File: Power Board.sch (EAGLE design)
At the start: 44 parts, among them IC1 SN74LS00N, Q1 IRLB8743PBF, U1 S18V20F12, U2 D24V22F3, U3 D24V22F5

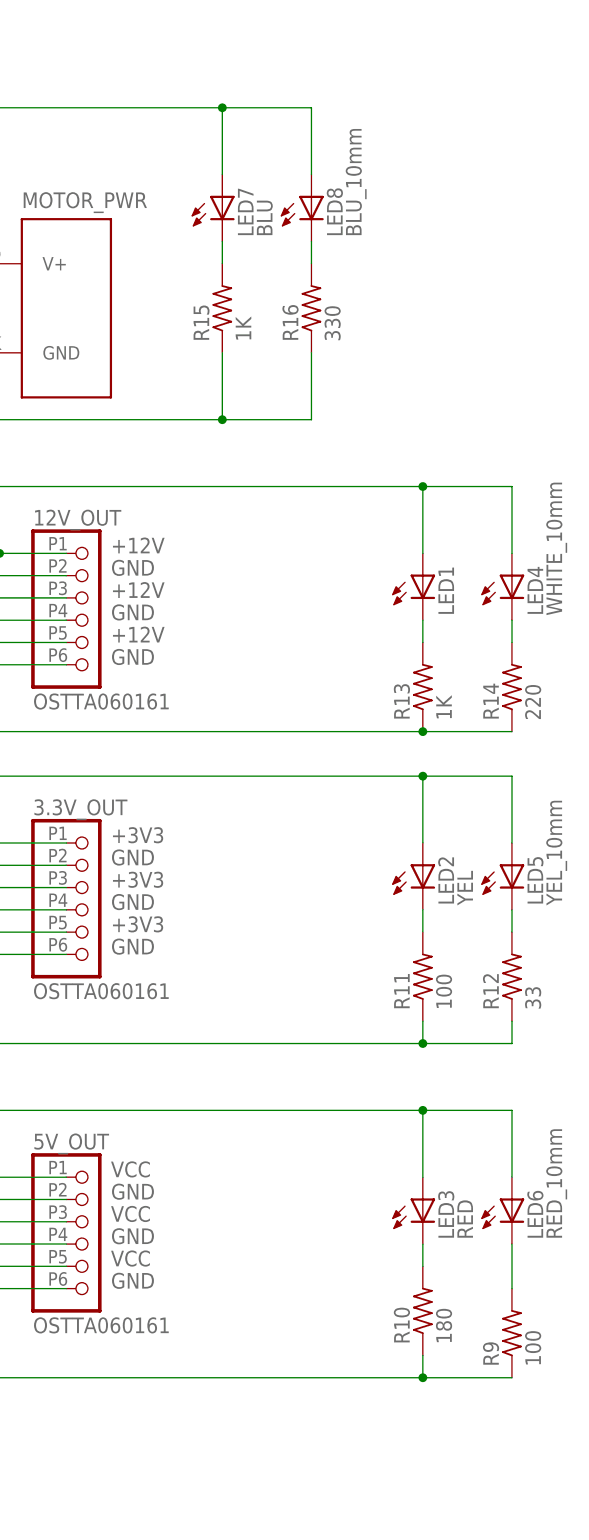
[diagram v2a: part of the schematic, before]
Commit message: Remove large LEDs (they were too hard to find, and produced too much heat)
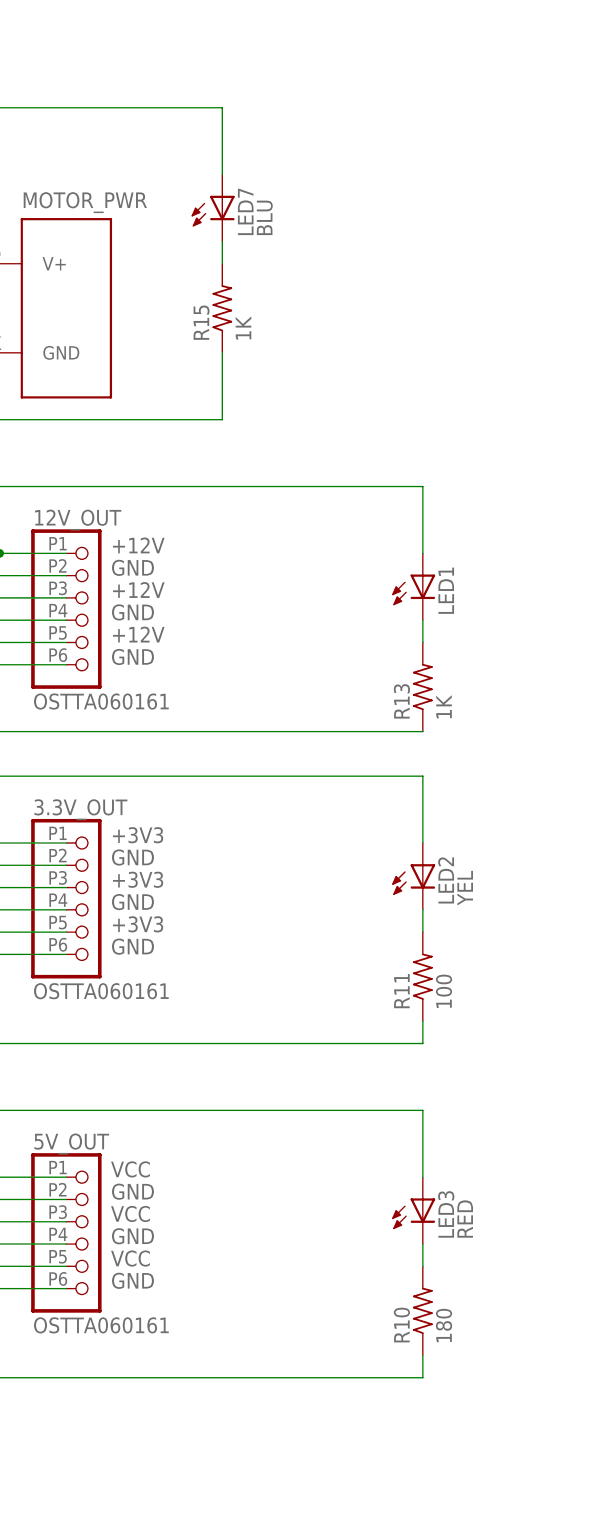
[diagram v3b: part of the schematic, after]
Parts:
- removed LED4: WHITE_10mm, led:LED10MM
- removed LED5: YEL_10mm, Power Board Custom:SPARKFUN_10MMLED
- removed LED6: RED_10mm, Power Board Custom:SPARKFUN_10MMLED
- removed LED8: BLU_10mm, led:LED10MM
- removed R12: 33, resistor:R-US_0207/10
- removed R14: 220, resistor:R-US_0207/10
- removed R16: 330, resistor:R-US_0207/10
- removed R9: 100, resistor:R-US_0207/10
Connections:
- removed net N$11: LED4.C, R14.2
- removed net N$14: LED8.C, R16.2
- removed net N$5: LED6.C, R9.2
- removed net N$9: LED5.C, R12.2
- net +12V: no longer LED4.A
- net +3V3: no longer LED5.A
- net GND: no longer R12.1, R14.1, R9.1
- net MOTOR_0V: no longer R16.1
- net MOTOR_V+: no longer LED8.A
- net VCC: no longer LED6.A
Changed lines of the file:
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@@
 <?xml version="1.0" encoding="utf-8"?>
 <!DOCTYPE eagle SYSTEM "eagle.dtd">
-<eagle version="8.4.0">
+<eagle version="8.6.1">
 <drawing>
 <settings>
-<setting alwaysvectorfont="no"/>
+<setting alwaysvectorfont="yes"/>
 <setting verticaltext="up"/>
 </settings>
@@
 <part name="LED2" library="led" library_urn="urn:adsk.eagle:library:259" deviceset="LED" device="5MM" package3d_urn="urn:adsk.eagle:package:15799/1" value="YEL"/>
 <part name="LED3" library="led" library_urn="urn:adsk.eagle:library:259" deviceset="LED" device="5MM" package3d_urn="urn:adsk.eagle:package:15799/1" value="RED"/>
-<part name="LED5" library="Power Board Custom" deviceset="SPARKFUN_10MMLED" device="" value="YEL_10mm"/>
-<part name="LED6" library="Power Board Custom" deviceset="SPARKFUN_10MMLED" device="" value="RED_10mm"/>
-<part name="R9" library="resistor" library_urn="urn:adsk.eagle:library:348" deviceset="R-US_" device="0207/10" package3d_urn="urn:adsk.eagle:package:25939/1" value="100"/>
 <part name="R10" library="resistor" library_urn="urn:adsk.eagle:library:348" deviceset="R-US_" device="0207/10" package3d_urn="urn:adsk.eagle:package:25939/1" value="180"/>
 <part name="R11" library="resistor" library_urn="urn:adsk.eagle:library:348" deviceset="R-US_" device="0207/10" package3d_urn="urn:adsk.eagle:package:25939/1" value="100"/>
-<part name="R12" library="resistor" library_urn="urn:adsk.eagle:library:348" deviceset="R-US_" device="0207/10" package3d_urn="urn:adsk.eagle:package:25939/1" value="33"/>
 <part name="R13" library="resistor" library_urn="urn:adsk.eagle:library:348" deviceset="R-US_" device="0207/10" package3d_urn="urn:adsk.eagle:package:25939/1" value="1K"/>
-<part name="R14" library="resistor" library_urn="urn:adsk.eagle:library:348" deviceset="R-US_" device="0207/10" package3d_urn="urn:adsk.eagle:package:25939/1" value="220"/>
 <part name="R15" library="resistor" library_urn="urn:adsk.eagle:library:348" deviceset="R-US_" device="0207/10" package3d_urn="urn:adsk.eagle:package:25939/1" value="1K"/>
-<part name="R16" library="resistor" library_urn="urn:adsk.eagle:library:348" deviceset="R-US_" device="0207/10" package3d_urn="urn:adsk.eagle:package:25939/1" value="330"/>
 <part name="LED7" library="led" library_urn="urn:adsk.eagle:library:259" deviceset="LED" device="5MM" package3d_urn="urn:adsk.eagle:package:15799/1" value="BLU"/>
-<part name="LED8" library="led" library_urn="urn:adsk.eagle:library:259" deviceset="LED" device="10MM" package3d_urn="urn:adsk.eagle:package:15828/1" value="BLU_10mm"/>
-<part name="LED4" library="led" library_urn="urn:adsk.eagle:library:259" deviceset="LED" device="10MM" package3d_urn="urn:adsk.eagle:package:15828/1" value="WHITE_10mm"/>
 </parts>
 <sheets>
@@
 <instance part="LED2" gate="G$1" x="236.22" y="132.08"/>
 <instance part="LED3" gate="G$1" x="236.22" y="93.98"/>
-<instance part="LED5" gate="G$1" x="246.38" y="132.08"/>
-<instance part="LED6" gate="G$1" x="246.38" y="93.98"/>
-<instance part="R9" gate="G$1" x="246.38" y="78.74" rot="R90"/>
 <instance part="R10" gate="G$1" x="236.22" y="81.28" rot="R90"/>
 <instance part="R11" gate="G$1" x="236.22" y="119.38" rot="R90"/>
-<instance part="R12" gate="G$1" x="246.38" y="119.38" rot="R90"/>
 <instance part="R13" gate="G$1" x="236.22" y="152.4" rot="R90"/>
-<instance part="R14" gate="G$1" x="246.38" y="152.4" rot="R90"/>
 <instance part="R15" gate="G$1" x="213.36" y="195.58" rot="R90"/>
-<instance part="R16" gate="G$1" x="223.52" y="195.58" rot="R90"/>
 <instance part="LED7" gate="G$1" x="213.36" y="208.28"/>
-<instance part="LED8" gate="G$1" x="223.52" y="208.28"/>
-<instance part="LED4" gate="G$1" x="246.38" y="165.1"/>
 </instances>
 <busses>
@@
 <wire x1="180.34" y1="73.66" x2="236.22" y2="73.66" width="0.1524" layer="91"/>
 <junction x="180.34" y="73.66"/>
-<pinref part="R9" gate="G$1" pin="1"/>
 <pinref part="R11" gate="G$1" pin="1"/>
-<wire x1="236.22" y1="73.66" x2="246.38" y2="73.66" width="0.1524" layer="91"/>
 <wire x1="236.22" y1="114.3" x2="236.22" y2="111.76" width="0.1524" layer="91"/>
 <wire x1="236.22" y1="111.76" x2="180.34" y2="111.76" width="0.1524" layer="91"/>
 <junction x="180.34" y="111.76"/>
-<pinref part="R12" gate="G$1" pin="1"/>
-<wire x1="246.38" y1="114.3" x2="246.38" y2="111.76" width="0.1524" layer="91"/>
-<wire x1="246.38" y1="111.76" x2="236.22" y2="111.76" width="0.1524" layer="91"/>
-<junction x="236.22" y="111.76"/>
 <pinref part="R13" gate="G$1" pin="1"/>
 <wire x1="236.22" y1="147.32" x2="180.34" y2="147.32" width="0.1524" layer="91"/>
 <junction x="180.34" y="147.32"/>
-<pinref part="R14" gate="G$1" pin="1"/>
-<wire x1="246.38" y1="147.32" x2="236.22" y2="147.32" width="0.1524" layer="91"/>
-<junction x="236.22" y="147.32"/>
 <pinref part="R10" gate="G$1" pin="1"/>
 <wire x1="236.22" y1="76.2" x2="236.22" y2="73.66" width="0.1524" layer="91"/>
-<junction x="236.22" y="73.66"/>
 </segment>
 <segment>
@@
 <wire x1="170.18" y1="218.44" x2="170.18" y2="200.66" width="0.1524" layer="91"/>
 <junction x="170.18" y="200.66"/>
-<pinref part="LED8" gate="G$1" pin="A"/>
-<wire x1="223.52" y1="210.82" x2="223.52" y2="218.44" width="0.1524" layer="91"/>
-<wire x1="223.52" y1="218.44" x2="213.36" y2="218.44" width="0.1524" layer="91"/>
-<junction x="213.36" y="218.44"/>
 </segment>
 </net>
@@
 <pinref part="LED1" gate="G$1" pin="A"/>
 <wire x1="236.22" y1="175.26" x2="236.22" y2="167.64" width="0.1524" layer="91"/>
-<wire x1="246.38" y1="167.64" x2="246.38" y2="175.26" width="0.1524" layer="91"/>
-<wire x1="246.38" y1="175.26" x2="236.22" y2="175.26" width="0.1524" layer="91"/>
-<junction x="236.22" y="175.26"/>
-<pinref part="LED4" gate="G$1" pin="A"/>
 </segment>
 </net>
@@
 <wire x1="182.88" y1="142.24" x2="182.88" y2="134.62" width="0.1524" layer="91"/>
 <junction x="182.88" y="134.62"/>
-<pinref part="LED5" gate="G$1" pin="A"/>
-<wire x1="246.38" y1="134.62" x2="246.38" y2="142.24" width="0.1524" layer="91"/>
-<wire x1="246.38" y1="142.24" x2="236.22" y2="142.24" width="0.1524" layer="91"/>
-<junction x="236.22" y="142.24"/>
 </segment>
 </net>
@@
 <wire x1="180.34" y1="182.88" x2="180.34" y2="190.5" width="0.1524" layer="91"/>
 <junction x="180.34" y="190.5"/>
-<pinref part="R16" gate="G$1" pin="1"/>
-<wire x1="223.52" y1="190.5" x2="223.52" y2="182.88" width="0.1524" layer="91"/>
-<wire x1="223.52" y1="182.88" x2="213.36" y2="182.88" width="0.1524" layer="91"/>
-<junction x="213.36" y="182.88"/>
 </segment>
 </net>
@@
 <wire x1="185.42" y1="104.14" x2="185.42" y2="96.52" width="0.1524" layer="91"/>
 <junction x="185.42" y="96.52"/>
-<pinref part="LED6" gate="G$1" pin="A"/>
-<wire x1="246.38" y1="96.52" x2="246.38" y2="104.14" width="0.1524" layer="91"/>
-<wire x1="246.38" y1="104.14" x2="236.22" y2="104.14" width="0.1524" layer="91"/>
-<junction x="236.22" y="104.14"/>
 </segment>
 <segment>
@@
 </segment>
 </net>
-<net name="N$5" class="0">
-<segment>
-<pinref part="R9" gate="G$1" pin="2"/>
-<pinref part="LED6" gate="G$1" pin="C"/>
-<wire x1="246.38" y1="83.82" x2="246.38" y2="88.9" width="0.1524" layer="91"/>
-</segment>
-</net>
 <net name="N$6" class="0">
 <segment>
@@
 </segment>
 </net>
-<net name="N$9" class="0">
-<segment>
-<pinref part="LED5" gate="G$1" pin="C"/>
-<pinref part="R12" gate="G$1" pin="2"/>
-<wire x1="246.38" y1="127" x2="246.38" y2="124.46" width="0.1524" layer="91"/>
-</segment>
-</net>
 <net name="N$10" class="0">
 <segment>
@@
 </segment>
 </net>
-<net name="N$11" class="0">
-<segment>
-<pinref part="R14" gate="G$1" pin="2"/>
-<wire x1="246.38" y1="160.02" x2="246.38" y2="157.48" width="0.1524" layer="91"/>
-<pinref part="LED4" gate="G$1" pin="C"/>
-</segment>
-</net>
 <net name="N$13" class="0">
 <segment>
@@
 </segment>
 </net>
-<net name="N$14" class="0">
-<segment>
-<pinref part="R16" gate="G$1" pin="2"/>
-<wire x1="223.52" y1="200.66" x2="223.52" y2="203.2" width="0.1524" layer="91"/>
-<pinref part="LED8" gate="G$1" pin="C"/>
-</segment>
-</net>
